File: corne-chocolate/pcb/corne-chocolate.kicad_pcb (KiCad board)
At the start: 2 copper layers, 133.8 x 91.4 mm, 98 parts, among them J3 LED, P1 i2c-pin, P2 i2c-pin, SW1 SW_PUSH, SW10 SW_PUSH, SW11 SW_PUSH, SW12 SW_PUSH, SW13 SW_PUSH, SW14 SW_PUSH, SW15 SW_PUSH, SW16 SW_PUSH, SW17 SW_PUSH, SW18 SW_PUSH, SW19 SW_PUSH, SW2 SW_PUSH, SW20 SW_PUSH, SW21 SW_PUSH, SW3 SW_PUSH, SW4 SW_PUSH, SW5 SW_PUSH, SW6 SW_PUSH, SW7 SW_PUSH, SW8 SW_PUSH, SW9 SW_PUSH, U1 ProMicro

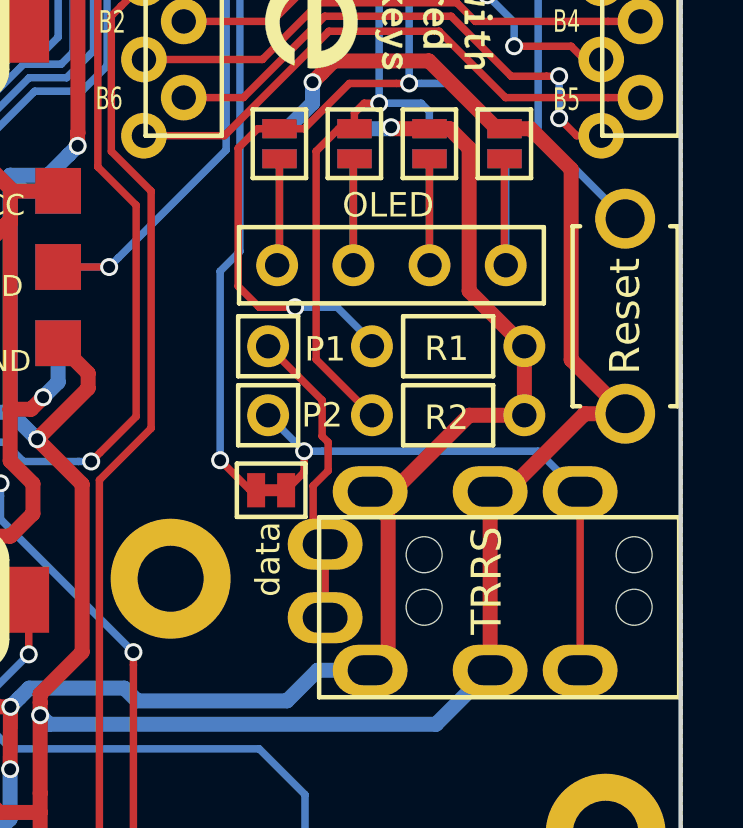
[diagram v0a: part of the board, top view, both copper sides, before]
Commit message: merge foostan libraries. ERC checked.
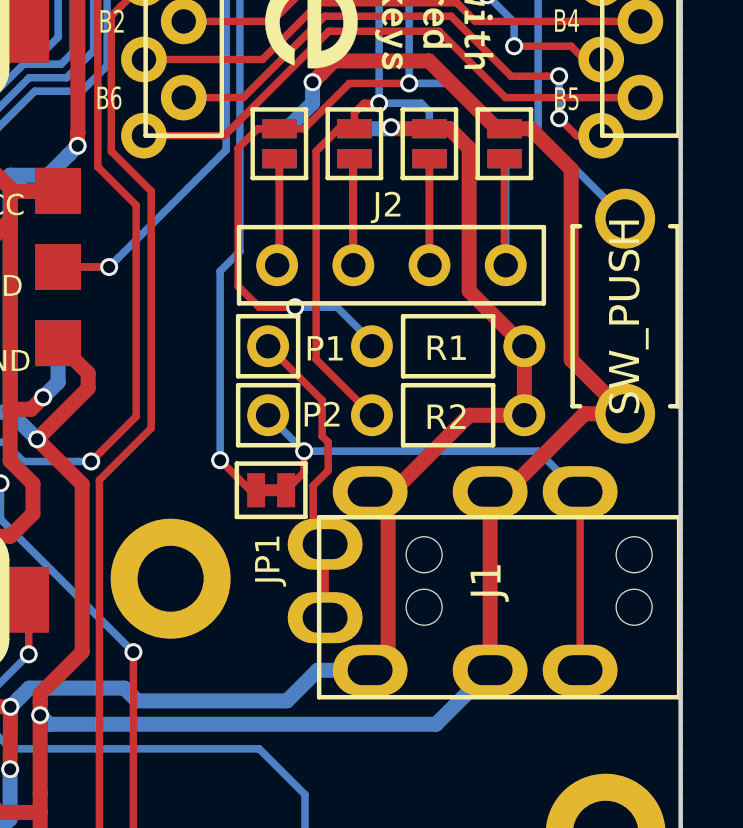
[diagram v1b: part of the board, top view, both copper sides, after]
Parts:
- J2: renamed from OLED; value OLED -> Conn_01x04
- RSW1: value Reset -> SW_PUSH
- renumbered TRRS to J1, data to JP1
